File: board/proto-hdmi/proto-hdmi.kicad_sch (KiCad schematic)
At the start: 1 part, among them J1 Conn_02x17_Odd_Even

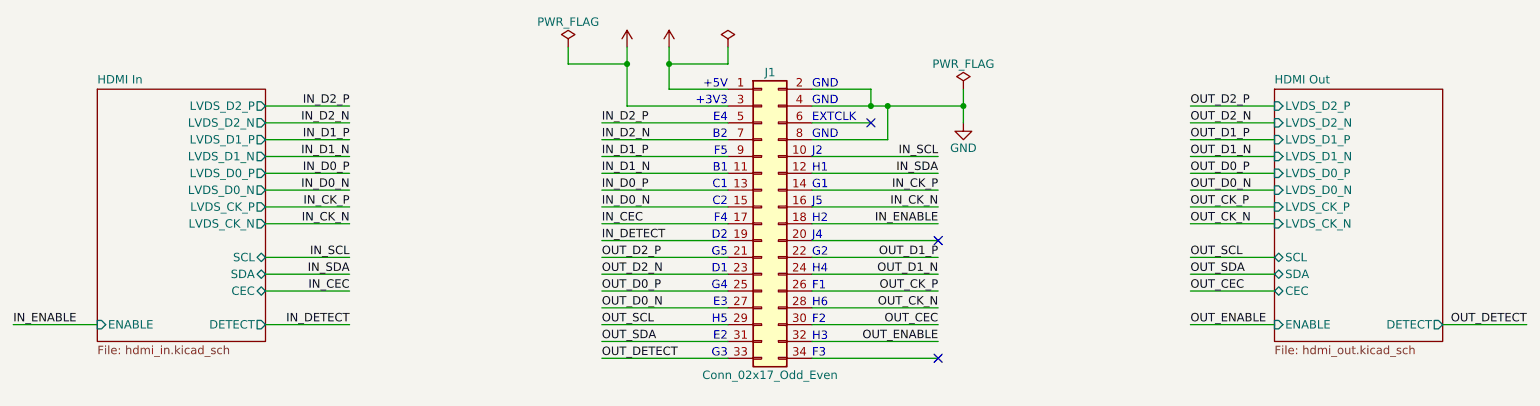
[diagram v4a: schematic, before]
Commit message: Connect source port hotplug detect.
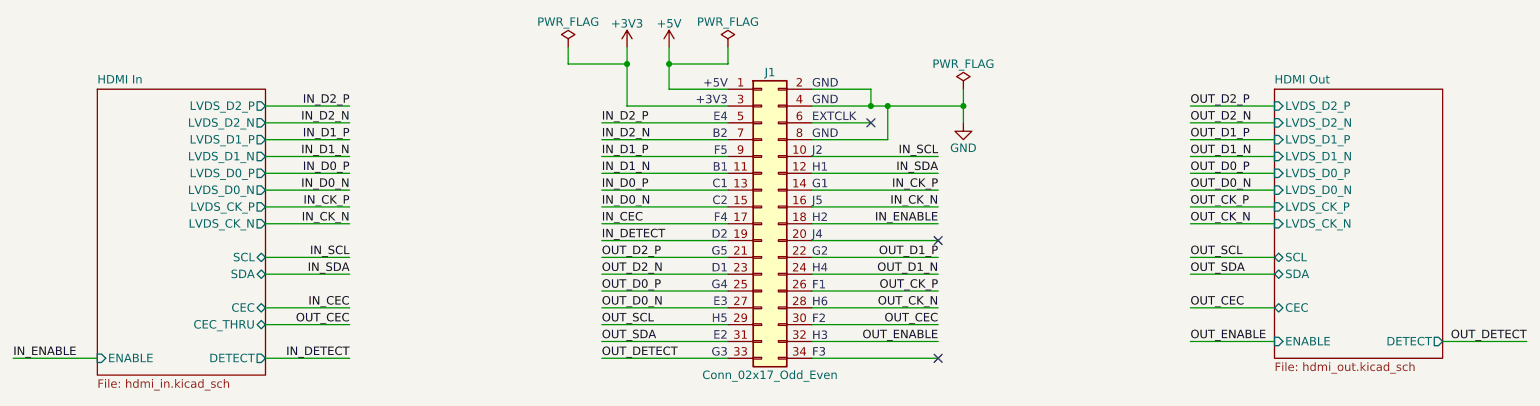
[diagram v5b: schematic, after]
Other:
- sheet HDMI In ports: added CEC_THRU; removed none
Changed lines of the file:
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@@
     (stroke (width 0) (type default) (color 0 0 0 0))
   )
-  (wire (pts (xy 241.3 86.36) (xy 254 86.36))
+  (wire (pts (xy 241.3 88.9) (xy 254 88.9))
     (stroke (width 0) (type default) (color 0 0 0 0))
   )
@@
     (stroke (width 0) (type default) (color 0 0 0 0))
   )
+  (wire (pts (xy 63.5 86.36) (xy 76.2 86.36))
+    (stroke (width 0) (type default) (color 0 0 0 0))
+  )
   (wire (pts (xy 215.9 58.42) (xy 203.2 58.42))
     (stroke (width 0) (type default) (color 0 0 0 0))
@@
     (stroke (width 0) (type default) (color 0 0 0 0))
   )
-  (wire (pts (xy 203.2 86.36) (xy 215.9 86.36))
+  (wire (pts (xy 203.2 88.9) (xy 215.9 88.9))
     (stroke (width 0) (type default) (color 0 0 0 0))
   )
@@
     (stroke (width 0) (type default) (color 0 0 0 0))
   )
-  (wire (pts (xy 63.5 81.28) (xy 76.2 81.28))
-    (stroke (width 0) (type default) (color 0 0 0 0))
-  )
-  (wire (pts (xy 203.2 81.28) (xy 215.9 81.28))
+  (wire (pts (xy 63.5 83.82) (xy 76.2 83.82))
+    (stroke (width 0) (type default) (color 0 0 0 0))
+  )
+  (wire (pts (xy 203.2 83.82) (xy 215.9 83.82))
     (stroke (width 0) (type default) (color 0 0 0 0))
   )
@@
     (stroke (width 0) (type default) (color 0 0 0 0))
   )
-  (wire (pts (xy 25.4 86.36) (xy 38.1 86.36))
-    (stroke (width 0) (type default) (color 0 0 0 0))
-  )
-  (wire (pts (xy 63.5 86.36) (xy 76.2 86.36))
+  (wire (pts (xy 25.4 91.44) (xy 38.1 91.44))
+    (stroke (width 0) (type default) (color 0 0 0 0))
+  )
+  (wire (pts (xy 63.5 91.44) (xy 76.2 91.44))
     (stroke (width 0) (type default) (color 0 0 0 0))
   )
@@
     (effects (font (size 1.27 1.27)) (justify left bottom))
   )
-  (label "OUT_ENABLE" (at 203.2 86.36 0)
+  (label "OUT_ENABLE" (at 203.2 88.9 0)
     (effects (font (size 1.27 1.27)) (justify left bottom))
   )
@@
     (effects (font (size 1.27 1.27)) (justify left bottom))
   )
-  (label "OUT_CEC" (at 203.2 81.28 0)
+  (label "OUT_CEC" (at 203.2 83.82 0)
     (effects (font (size 1.27 1.27)) (justify left bottom))
   )
@@
     (effects (font (size 1.27 1.27)) (justify right bottom))
   )
-  (label "IN_DETECT" (at 76.2 86.36 180)
+  (label "IN_DETECT" (at 76.2 91.44 180)
     (effects (font (size 1.27 1.27)) (justify right bottom))
   )
@@
     (effects (font (size 1.27 1.27)) (justify right bottom))
   )
-  (label "OUT_DETECT" (at 254 86.36 180)
+  (label "OUT_DETECT" (at 254 88.9 180)
     (effects (font (size 1.27 1.27)) (justify right bottom))
   )
@@
     (effects (font (size 1.27 1.27)) (justify right bottom))
   )
+  (label "OUT_CEC" (at 76.2 86.36 180)
+    (effects (font (size 1.27 1.27)) (justify right bottom))
+  )
   (label "OUT_D2_N" (at 203.2 55.88 0)
     (effects (font (size 1.27 1.27)) (justify left bottom))
@@
     (effects (font (size 1.27 1.27)) (justify left bottom))
   )
-  (label "IN_ENABLE" (at 25.4 86.36 0)
+  (label "IN_ENABLE" (at 25.4 91.44 0)
     (effects (font (size 1.27 1.27)) (justify left bottom))
   )
@@
     (effects (font (size 1.27 1.27)) (justify right bottom))
   )
-  (label "IN_CEC" (at 76.2 81.28 180)
+  (label "IN_CEC" (at 76.2 83.82 180)
     (effects (font (size 1.27 1.27)) (justify right bottom))
   )
@@
       (effects (font (size 1.27 1.27)) hide)
     )
-    (property "Value" "" (id 1) (at 124.46 40.894 0))
+    (property "Value" "+5V" (id 1) (at 124.46 40.894 0))
     (property "Footprint" "" (id 2) (at 124.46 44.45 0)
       (effects (font (size 1.27 1.27)) hide)
@@
       (effects (font (size 1.27 1.27)) hide)
     )
-    (property "Value" "" (id 1) (at 118.11 40.894 0))
+    (property "Value" "+3V3" (id 1) (at 118.11 40.894 0))
     (property "Footprint" "" (id 2) (at 118.11 44.45 0)
       (effects (font (size 1.27 1.27)) hide)
@@
       (effects (font (size 1.27 1.27)) hide)
     )
-    (property "Value" "" (id 1) (at 133.35 40.64 0))
+    (property "Value" "PWR_FLAG" (id 1) (at 133.35 40.64 0))
     (property "Footprint" "" (id 2) (at 133.35 44.45 0)
       (effects (font (size 1.27 1.27)) hide)
@@
     (pin "1")
   )
-  (sheet (at 215.9 50.8) (size 25.4 38.1) (fields_autoplaced)
+  (sheet (at 215.9 50.8) (size 25.4 40.64) (fields_autoplaced)
     (stroke (width 0.1524) (type solid) (color 0 0 0 0))
     (fill (color 0 0 0 0.0000))
@@
       (effects (font (size 1.27 1.27)) (justify left bottom))
     )
-    (property "Sheet file" "hdmi_out.kicad_sch" (id 1) (at 215.9 89.4846 0)
+    (property "Sheet file" "hdmi_out.kicad_sch" (id 1) (at 215.9 92.0246 0)
       (effects (font (size 1.27 1.27)) (justify left top))
     )
@@
       (effects (font (size 1.27 1.27)) (justify left))
     )
-    (pin "ENABLE" input (at 215.9 86.36 180)
-      (effects (font (size 1.27 1.27)) (justify left))
-    )
-    (pin "CEC" bidirectional (at 215.9 81.28 180)
-      (effects (font (size 1.27 1.27)) (justify left))
-    )
-    (pin "DETECT" output (at 241.3 86.36 0)
-      (effects (font (size 1.27 1.27)) (justify right))
-    )
-  )
-  (sheet (at 38.1 50.8) (size 25.4 38.1) (fields_autoplaced)
+    (pin "ENABLE" input (at 215.9 88.9 180)
+      (effects (font (size 1.27 1.27)) (justify left))
+    )
+    (pin "CEC" bidirectional (at 215.9 83.82 180)
+      (effects (font (size 1.27 1.27)) (justify left))
+    )
+    (pin "DETECT" output (at 241.3 88.9 0)
+      (effects (font (size 1.27 1.27)) (justify right))
+    )
+  )
+  (sheet (at 38.1 50.8) (size 25.4 43.18) (fields_autoplaced)
     (stroke (width 0.1524) (type solid) (color 0 0 0 0))
     (fill (color 0 0 0 0.0000))
@@
       (effects (font (size 1.27 1.27)) (justify left bottom))
     )
-    (property "Sheet file" "hdmi_in.kicad_sch" (id 1) (at 38.1 89.4846 0)
+    (property "Sheet file" "hdmi_in.kicad_sch" (id 1) (at 38.1 94.5646 0)
       (effects (font (size 1.27 1.27)) (justify left top))
     )
@@
       (effects (font (size 1.27 1.27)) (justify right))
     )
-    (pin "ENABLE" input (at 38.1 86.36 180)
-      (effects (font (size 1.27 1.27)) (justify left))
-    )
-    (pin "CEC" bidirectional (at 63.5 81.28 0)
-      (effects (font (size 1.27 1.27)) (justify right))
-    )
-    (pin "DETECT" output (at 63.5 86.36 0)
+    (pin "ENABLE" input (at 38.1 91.44 180)
+      (effects (font (size 1.27 1.27)) (justify left))
+    )
+    (pin "CEC" bidirectional (at 63.5 83.82 0)
+      (effects (font (size 1.27 1.27)) (justify right))
+    )
+    (pin "DETECT" output (at 63.5 91.44 0)
+      (effects (font (size 1.27 1.27)) (justify right))
+    )
+    (pin "CEC_THRU" bidirectional (at 63.5 86.36 0)
       (effects (font (size 1.27 1.27)) (justify right))
     )
@@
       (reference "#PWR0116") (unit 1) (value "GND") (footprint "")
     )
+    (path "/90192fd6-a099-42f6-a4b6-db64a36163fa/c21fbb5f-3d70-47e1-bca8-ccff68264d74"
+      (reference "#PWR0117") (unit 1) (value "+3V3") (footprint "")
+    )
     (path "/90192fd6-a099-42f6-a4b6-db64a36163fa/ff90cf5c-6dda-4a54-a626-934b7ed0a170"
       (reference "#PWR0118") (unit 1) (value "GND") (footprint "")
@@
       (reference "#PWR0119") (unit 1) (value "+3V3") (footprint "")
     )
+    (path "/90192fd6-a099-42f6-a4b6-db64a36163fa/a115b7aa-3872-45bc-abff-1b8f1defec8f"
+      (reference "#PWR0120") (unit 1) (value "GND") (footprint "")
+    )
     (path "/90192fd6-a099-42f6-a4b6-db64a36163fa/9de6b0a9-ef1a-41ae-81c0-eed13db383f8"
       (reference "C1") (unit 1) (value "C") (footprint "Capacitor_SMD:C_0402_1005Metric")
@@
     )
     (path "/90192fd6-a099-42f6-a4b6-db64a36163fa/a627ab25-ba94-4b85-80e0-61cf2e292a55"
-      (reference "U1") (unit 1) (value "NXP_NTS0302") (footprint "Package_SON:X2SON-8_1.4x1mm_P0.35mm")
+      (reference "U1") (unit 1) (value "NTS0302") (footprint "Package_SON:X2SON-8_1.4x1mm_P0.35mm")
     )
     (path "/0835e5dd-07f6-4583-955d-96fe9bbb7c49/3c65857a-cd94-4bda-aed7-27a2de6a0cfe"
@@
       (reference "U3") (unit 1) (value "M24C02") (footprint "0Local:ST_UFDFPN5")
     )
-  )
+    (path "/90192fd6-a099-42f6-a4b6-db64a36163fa/1fa6f1b9-529a-4dac-bbd8-3b3781adeb26"
+      (reference "U4") (unit 1) (value "74LVC1G17") (footprint "Package_TO_SOT_SMD:SOT-886")
+    )
+  )

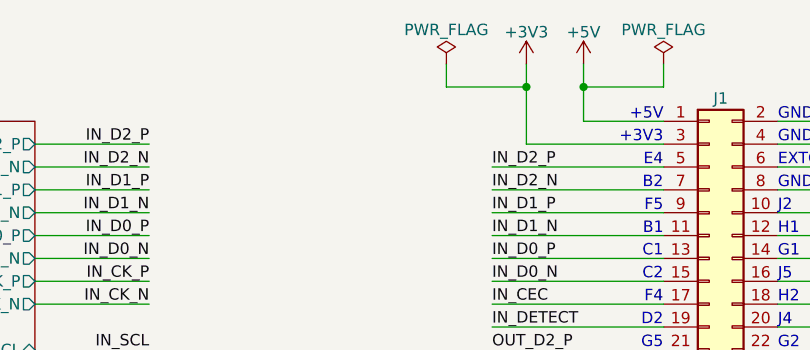
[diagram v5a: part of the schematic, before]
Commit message: Set up most of the non-TMDS source stuff.
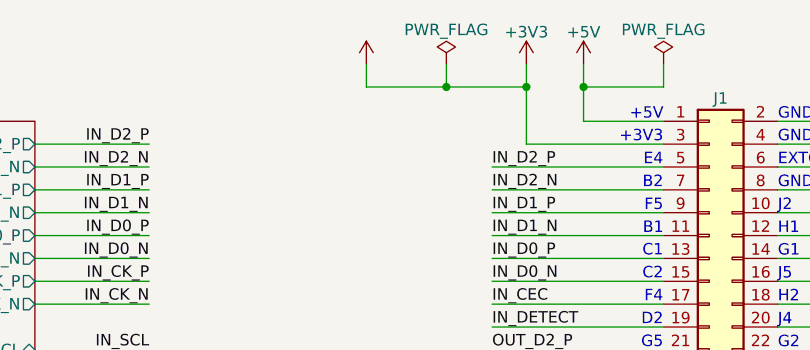
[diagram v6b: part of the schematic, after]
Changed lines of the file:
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@@
     (comment 1 "https://github.com/Elemecca/1240pi")
+  )
+  (junction (at 109.22 46.99) (diameter 0) (color 0 0 0 0)
   )
   (junction (at 124.46 46.99) (diameter 0) (color 0 0 0 0)
@@
     (stroke (width 0) (type default) (color 0 0 0 0))
   )
+  (wire (pts (xy 100.33 44.45) (xy 100.33 46.99))
+    (stroke (width 0) (type default) (color 0 0 0 0))
+  )
   (wire (pts (xy 114.3 66.04) (xy 133.35 66.04))
     (stroke (width 0) (type default) (color 0 0 0 0))
@@
   )
   (wire (pts (xy 114.3 81.28) (xy 133.35 81.28))
+    (stroke (width 0) (type default) (color 0 0 0 0))
+  )
+  (wire (pts (xy 100.33 46.99) (xy 109.22 46.99))
     (stroke (width 0) (type default) (color 0 0 0 0))
   )
@@
     (pin "1")
   )
+  (symbol (lib_id "power:VCC") (at 100.33 44.45 0) (unit 1)
+    (in_bom yes) (on_board yes)
+    (property "Reference" "#PWR0117" (id 0) (at 100.33 48.26 0)
+      (effects (font (size 1.27 1.27)) hide)
+    )
+    (property "Value" "" (id 1) (at 100.33 40.64 0))
+    (property "Footprint" "" (id 2) (at 100.33 44.45 0)
+      (effects (font (size 1.27 1.27)) hide)
+    )
+    (property "Datasheet" "" (id 3) (at 100.33 44.45 0)
+      (effects (font (size 1.27 1.27)) hide)
+    )
+    (pin "1")
+  )
   (symbol (lib_id "power:PWR_FLAG") (at 109.22 44.45 0) (unit 1)
     (in_bom yes) (on_board yes)
@@
       (reference "#PWR0116") (unit 1) (value "GND") (footprint "")
     )
-    (path "/90192fd6-a099-42f6-a4b6-db64a36163fa/c21fbb5f-3d70-47e1-bca8-ccff68264d74"
-      (reference "#PWR0117") (unit 1) (value "+3V3") (footprint "")
+    (path "/e27a5311-ec83-49df-9b19-dfad7d43f9b4"
+      (reference "#PWR0117") (unit 1) (value "VCC") (footprint "")
     )
     (path "/90192fd6-a099-42f6-a4b6-db64a36163fa/ff90cf5c-6dda-4a54-a626-934b7ed0a170"
@@
       (reference "#PWR0119") (unit 1) (value "+3V3") (footprint "")
     )
-    (path "/90192fd6-a099-42f6-a4b6-db64a36163fa/a115b7aa-3872-45bc-abff-1b8f1defec8f"
+    (path "/0835e5dd-07f6-4583-955d-96fe9bbb7c49/59886fdd-3e8e-4a71-bcfe-0370ac72c009"
       (reference "#PWR0120") (unit 1) (value "GND") (footprint "")
+    )
+    (path "/0835e5dd-07f6-4583-955d-96fe9bbb7c49/5033dfb3-7d47-4798-beae-259ad70427d5"
+      (reference "#PWR0121") (unit 1) (value "+3V3") (footprint "")
+    )
+    (path "/0835e5dd-07f6-4583-955d-96fe9bbb7c49/74754828-c83e-4495-b82f-d5e80574b346"
+      (reference "#PWR0122") (unit 1) (value "GND") (footprint "")
+    )
+    (path "/0835e5dd-07f6-4583-955d-96fe9bbb7c49/06d60174-874b-4319-9e8b-a82049cf4f12"
+      (reference "#PWR0123") (unit 1) (value "+5V") (footprint "")
     )
     (path "/90192fd6-a099-42f6-a4b6-db64a36163fa/9de6b0a9-ef1a-41ae-81c0-eed13db383f8"
@@
       (reference "C8") (unit 1) (value "C") (footprint "Capacitor_SMD:C_0402_1005Metric")
     )
+    (path "/0835e5dd-07f6-4583-955d-96fe9bbb7c49/d72064af-efea-4d78-8075-3484f295eac2"
+      (reference "C9") (unit 1) (value "22u") (footprint "Capacitor_SMD:C_0402_1005Metric")
+    )
+    (path "/0835e5dd-07f6-4583-955d-96fe9bbb7c49/ce62eb64-1eac-449e-bf08-93978d6d2d74"
+      (reference "C10") (unit 1) (value "1u") (footprint "Capacitor_SMD:C_0402_1005Metric")
+    )
+    (path "/0835e5dd-07f6-4583-955d-96fe9bbb7c49/fe0354ad-03fc-46c3-88a4-4ff4ca27971d"
+      (reference "C11") (unit 1) (value "10u") (footprint "Capacitor_SMD:C_0402_1005Metric")
+    )
     (path "/90192fd6-a099-42f6-a4b6-db64a36163fa/e351ba64-b0e1-40cc-a8b1-b31fd7d50e33"
       (reference "D1") (unit 1) (value "SBA0520Q") (footprint "Diode_SMD:D_0402_1005Metric")
@@
       (reference "D2") (unit 1) (value "SBA0520Q") (footprint "Diode_SMD:D_0402_1005Metric")
     )
+    (path "/0835e5dd-07f6-4583-955d-96fe9bbb7c49/2365fc84-1b87-47be-9d78-4a00fa92c9b9"
+      (reference "D3") (unit 1) (value "SBA0520Q") (footprint "Diode_SMD:D_0402_1005Metric")
+    )
     (path "/825ebd4a-7ae1-40e7-97f8-b2b2d0f262c8"
       (reference "J1") (unit 1) (value "Conn_02x17_Odd_Even") (footprint "Connector_PinSocket_2.54mm:PinSocket_2x17_P2.54mm_Horizontal")
@@
       (reference "R29") (unit 1) (value "1k") (footprint "Resistor_SMD:R_0402_1005Metric")
     )
+    (path "/0835e5dd-07f6-4583-955d-96fe9bbb7c49/8fe564dd-684d-4655-b2f6-b723ab5df147"
+      (reference "R30") (unit 1) (value "412R") (footprint "Resistor_SMD:R_0402_1005Metric")
+    )
+    (path "/0835e5dd-07f6-4583-955d-96fe9bbb7c49/9cb73762-45fc-48a8-a173-0620fc3cf36f"
+      (reference "R31") (unit 1) (value "2k") (footprint "Resistor_SMD:R_0402_1005Metric")
+    )
+    (path "/0835e5dd-07f6-4583-955d-96fe9bbb7c49/b3a2e9a1-e1b1-40f6-85a4-b7089d6334a8"
+      (reference "R32") (unit 1) (value "2k") (footprint "Resistor_SMD:R_0402_1005Metric")
+    )
+    (path "/0835e5dd-07f6-4583-955d-96fe9bbb7c49/6b507798-2f22-4cd6-a10c-0e87f748e3e2"
+      (reference "R33") (unit 1) (value "47k") (footprint "Resistor_SMD:R_0402_1005Metric")
+    )
+    (path "/0835e5dd-07f6-4583-955d-96fe9bbb7c49/b8cdb2b6-6d78-4d2e-bfe1-23896136ea76"
+      (reference "R34") (unit 1) (value "27k") (footprint "Resistor_SMD:R_0402_1005Metric")
+    )
+    (path "/0835e5dd-07f6-4583-955d-96fe9bbb7c49/35c4fd92-78b0-475c-951e-e82ee3cf7a8a"
+      (reference "R35") (unit 1) (value "10k") (footprint "Resistor_SMD:R_0402_1005Metric")
+    )
     (path "/90192fd6-a099-42f6-a4b6-db64a36163fa/dda43735-eab6-45e8-9372-ffd00ce32c09"
       (reference "SW1") (unit 1) (value "CTS_218-4LPSTR") (footprint "0Local:CTS_218-4")
@@
       (reference "U4") (unit 1) (value "74LVC1G17") (footprint "Package_TO_SOT_SMD:SOT-886")
     )
-  )
+    (path "/0835e5dd-07f6-4583-955d-96fe9bbb7c49/a28126d2-5e71-481d-ad50-99669a2d3691"
+      (reference "U5") (unit 1) (value "MIC2097-1") (footprint "0Local:Package_TMLF-6_EP_1.6mm")
+    )
+    (path "/0835e5dd-07f6-4583-955d-96fe9bbb7c49/94923077-9c47-4e66-8c91-e8e3b3ce23a7"
+      (reference "U6") (unit 1) (value "74LVC1G17") (footprint "Package_TO_SOT_SMD:SOT-886")
+    )
+  )

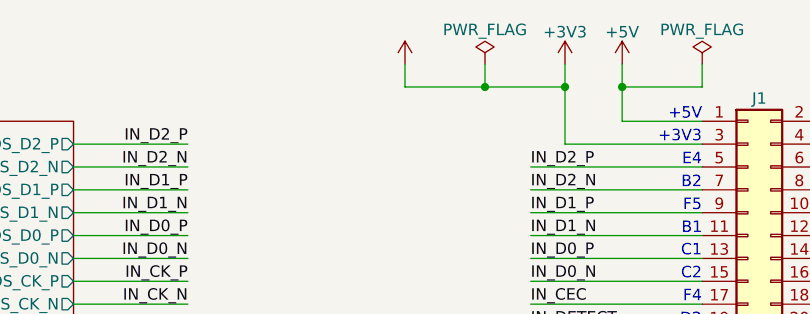
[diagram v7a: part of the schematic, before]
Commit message: Fix DRC issues on HDMI board.
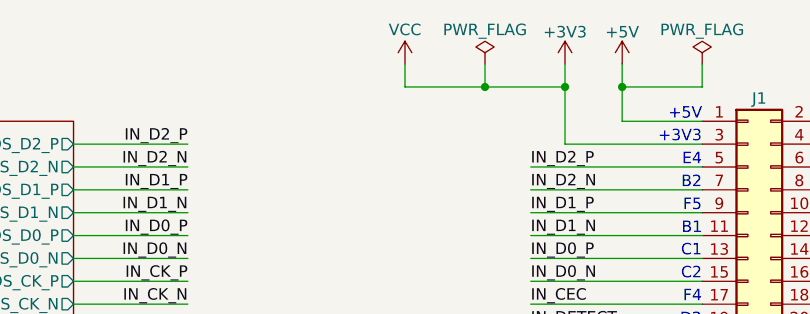
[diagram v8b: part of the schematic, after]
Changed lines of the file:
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@@
       (effects (font (size 1.27 1.27)) hide)
     )
-    (property "Value" "" (id 1) (at 100.33 40.64 0))
+    (property "Value" "VCC" (id 1) (at 100.33 40.64 0))
     (property "Footprint" "" (id 2) (at 100.33 44.45 0)
       (effects (font (size 1.27 1.27)) hide)
